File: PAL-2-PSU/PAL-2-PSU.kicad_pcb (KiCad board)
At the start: 2 copper layers, 74.1 x 79.3 mm, 20 parts, among them J1 Application Connector, J2 +5V, J3 Serial-8, J4 I/O, J5 RS232, SW1 Power, SW2 DECODE_EN, SW3 INPUT, SW4 TTY, U1 MAX202

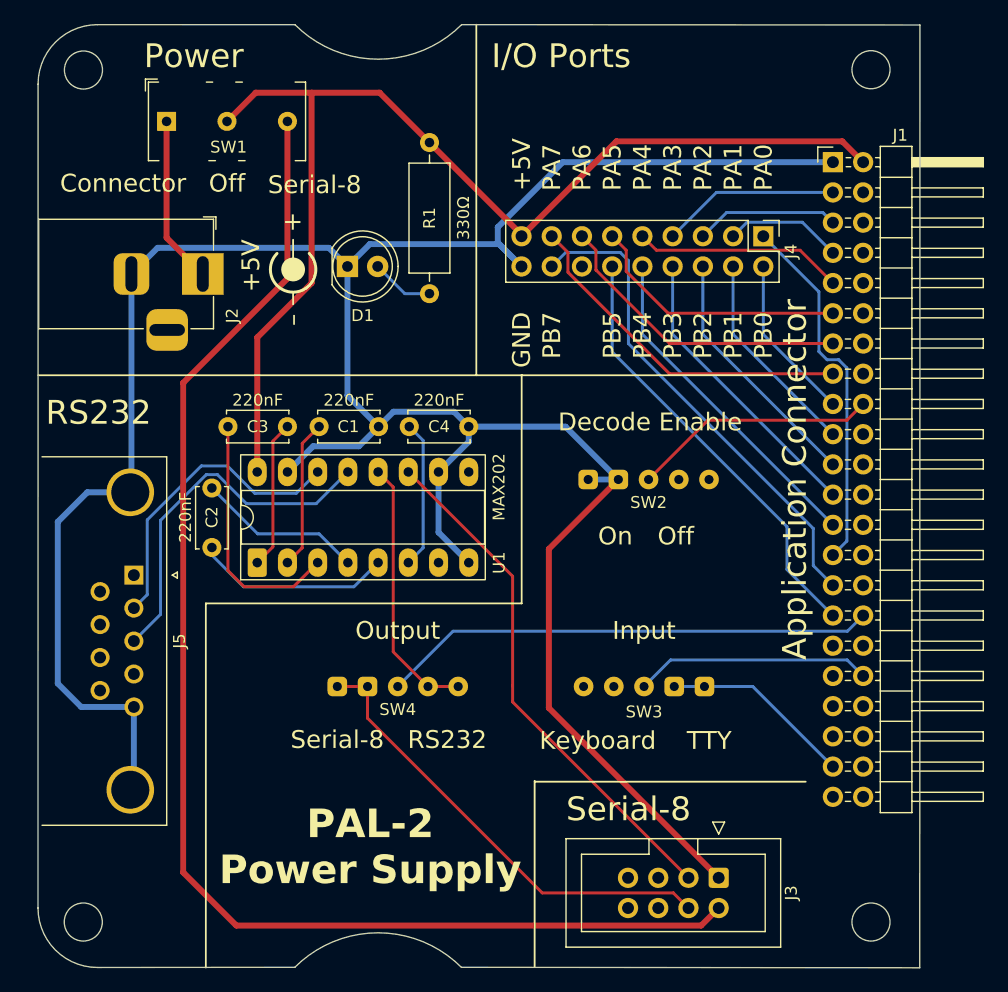
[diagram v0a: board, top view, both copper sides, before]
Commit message: Use 2.54/5.08mm footprint for power switch.
Label Serial-8 pins.
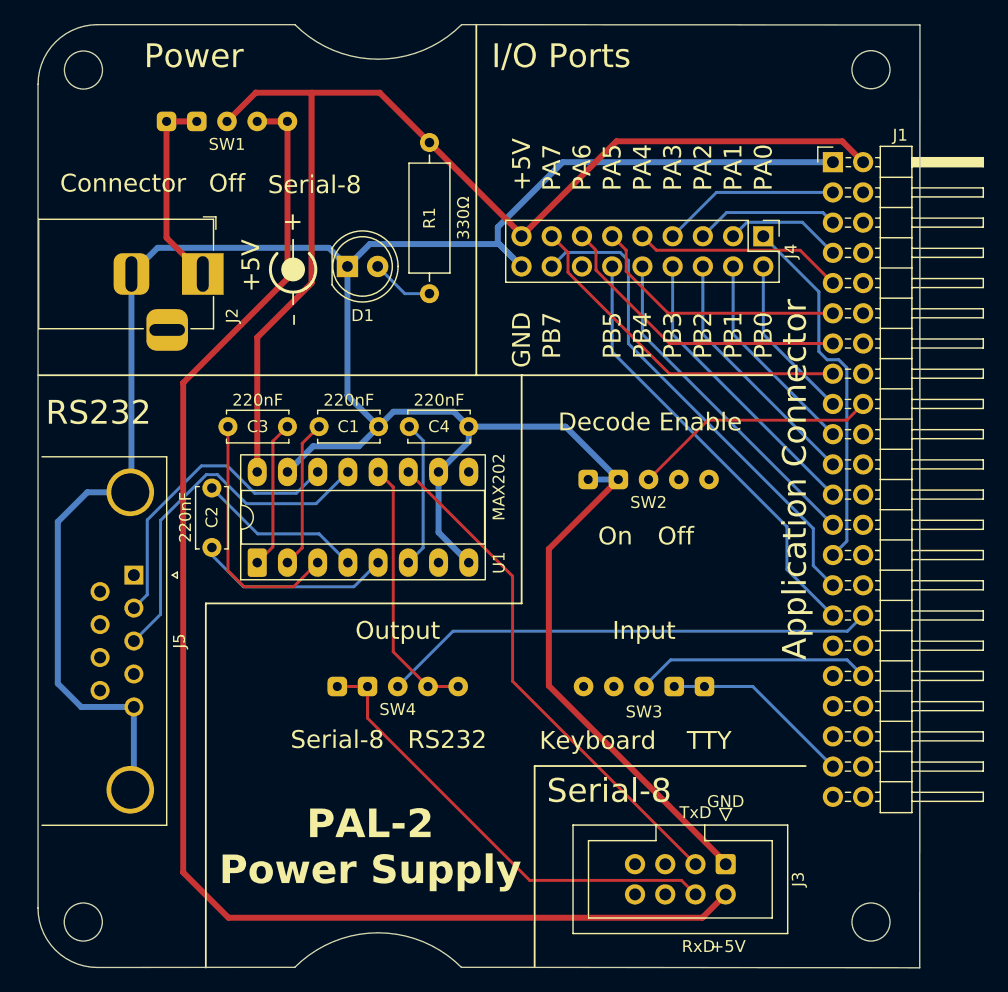
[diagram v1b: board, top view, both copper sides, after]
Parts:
- SW1: footprint T-Pau:SS-25139-NH -> T-Pau:SW-2.54-5.08
- moved SW1 6.91 mm to (79.4, 43.0)
- moved J3 1.29 mm to (121.3, 98.5)
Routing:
- net +5V Serial-8: track 114.2 -> 117.3 mm
- net /+5V Connector: track 14.1 -> 16.6 mm
- net TxD: track 43.9 -> 43.0 mm
- net GND: track 228.6 -> 227.7 mm
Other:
- board text added: "RxD"
- board text added: "TxD"

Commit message: Fix missing trace, make switch positions more logical.
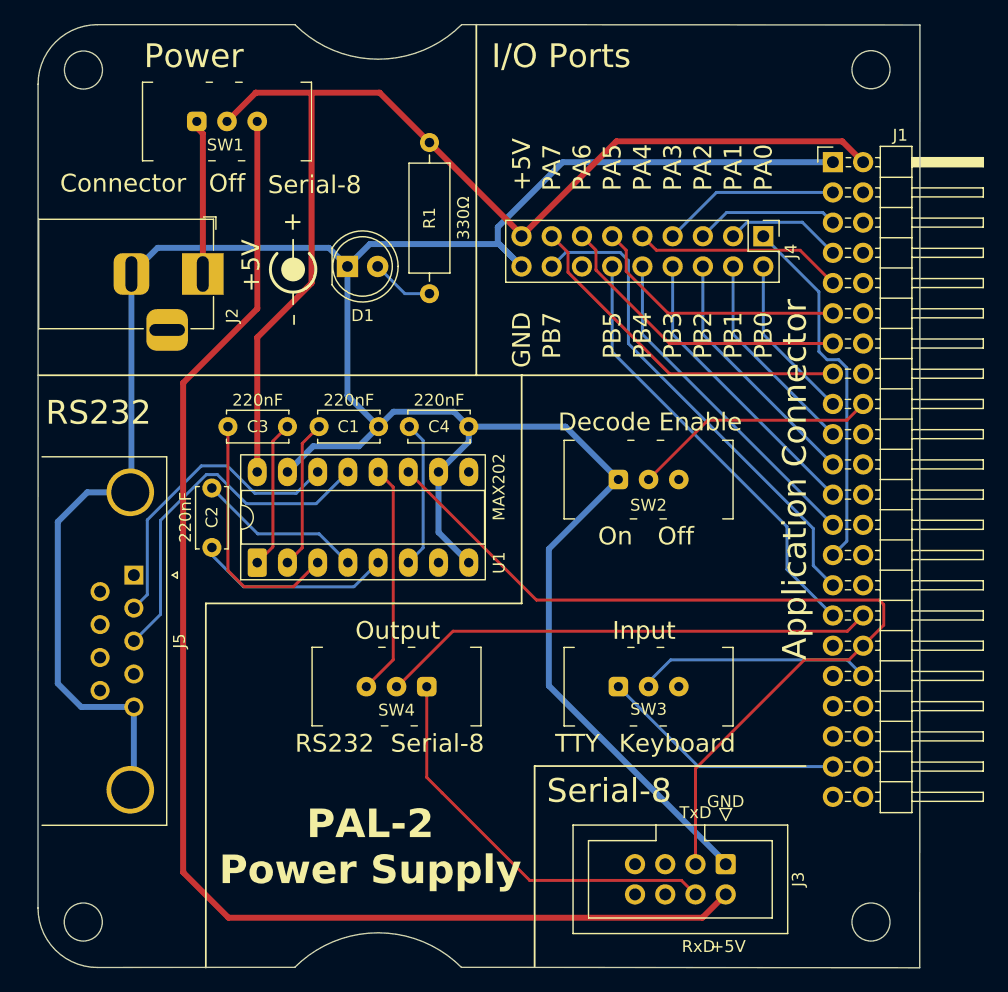
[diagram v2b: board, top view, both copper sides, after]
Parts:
- SW1, SW2, SW3, SW4: footprint T-Pau:SW-2.54-5.08 -> T-Pau:SS2513
- moved SW3 13.8 mm to (114.8, 90.5), turned to 0 degrees
- moved SW4 13.8 mm to (93.6, 76.7), turned to 180 degrees
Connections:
- net KYBD renamed RxD
- J1 pad U: PTR -> TxD
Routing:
- net TxD: track 43.0 -> 75.2 mm
- net KB_COL_A: track 16.1 -> 20.8 mm
- net RxD Serial-8: track 38.9 -> 34.3 mm
- net /+5V Connector: track 16.6 -> 13.0 mm
- net +5V Serial-8: track 117.3 -> 113.7 mm
- net RxD RSS: track 22.3 -> 19.5 mm
- net GND: track 227.7 -> 225.1 mm
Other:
- board text added: "PAL-2 Power Supply Revision 2 ©2025 Dieter Baron github.com/T-Pau/PAL-2-PSU"
- board text removed: "PAL-2 Power Supply Revision 1 ©2025 Dieter Baron github.com/T-Pau/PAL-2-PSU"
